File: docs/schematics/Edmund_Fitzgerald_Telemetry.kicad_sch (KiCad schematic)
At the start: 18 parts, among them J1 RC_Receiver, J3 Battery_LiPo, M1 Rudder_Servo, Q1 MOSFET_N, Q2 MOSFET_N, U1 ESP32_Control, U2 MAX98357A, U3 DFPlayer_Pro, U4 ESP32-CAM, U5 UBEC_5V_3A

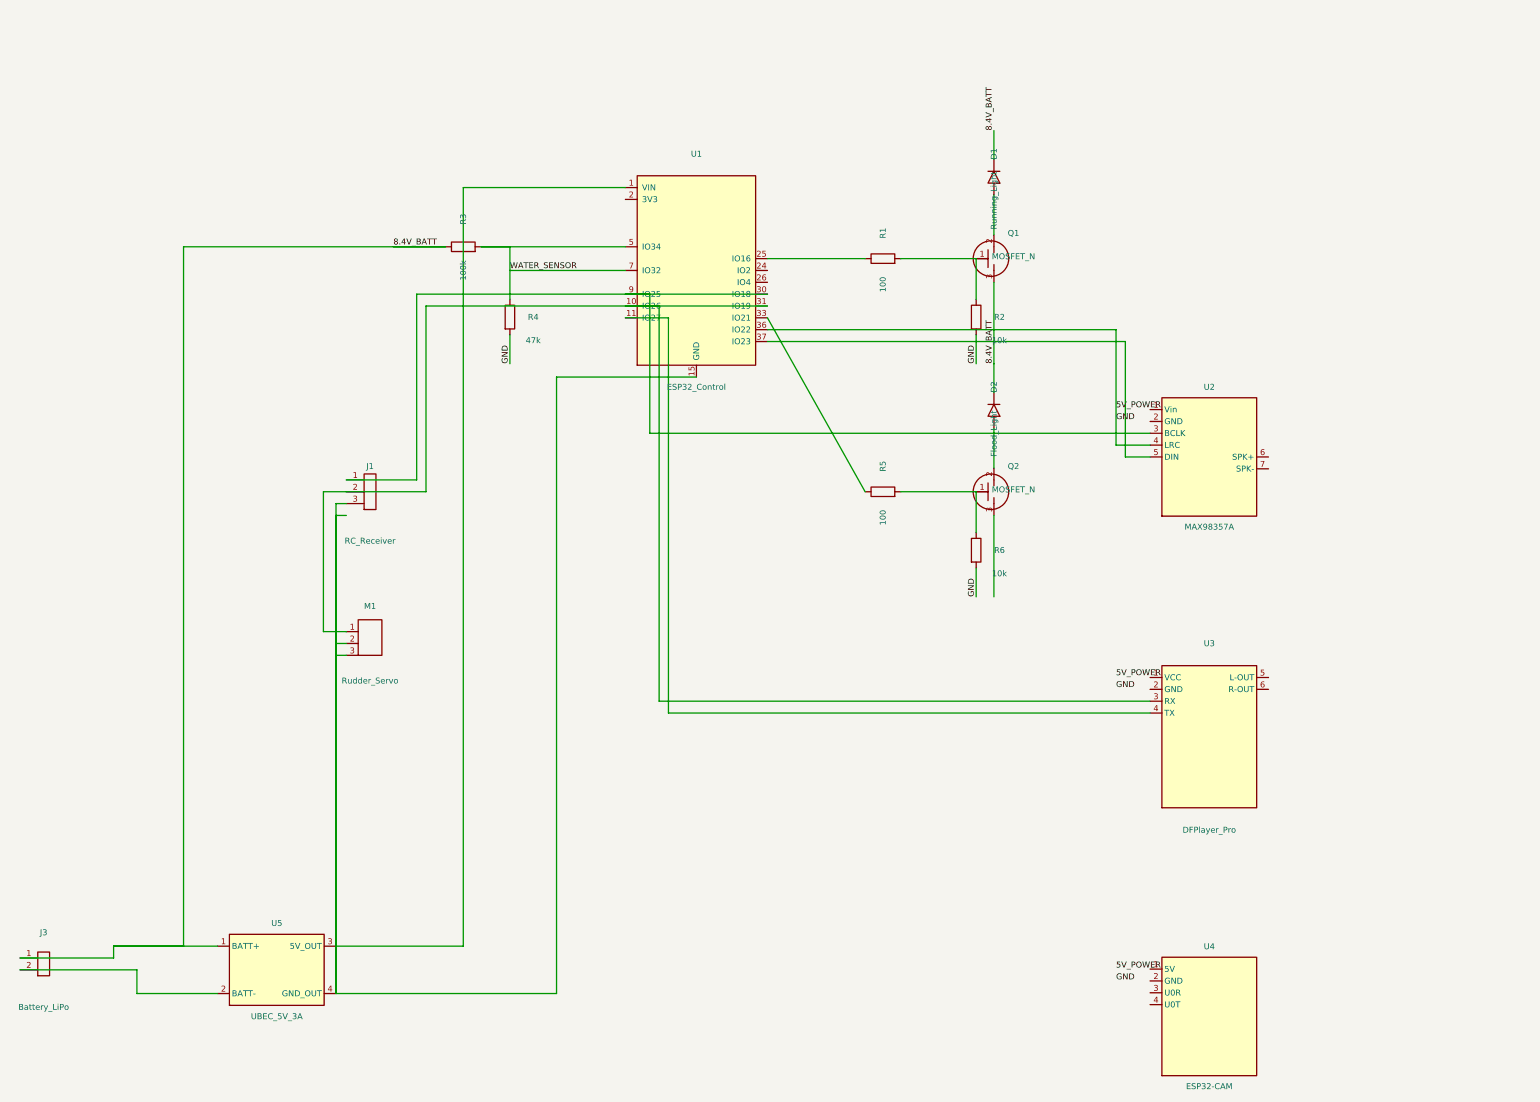
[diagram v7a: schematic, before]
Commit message: Website update: Integrated updated system schematic
- Verified schematic PNG integration in Design and Schematics section
- Committed latest KiCAD schematic source file (v6.0)
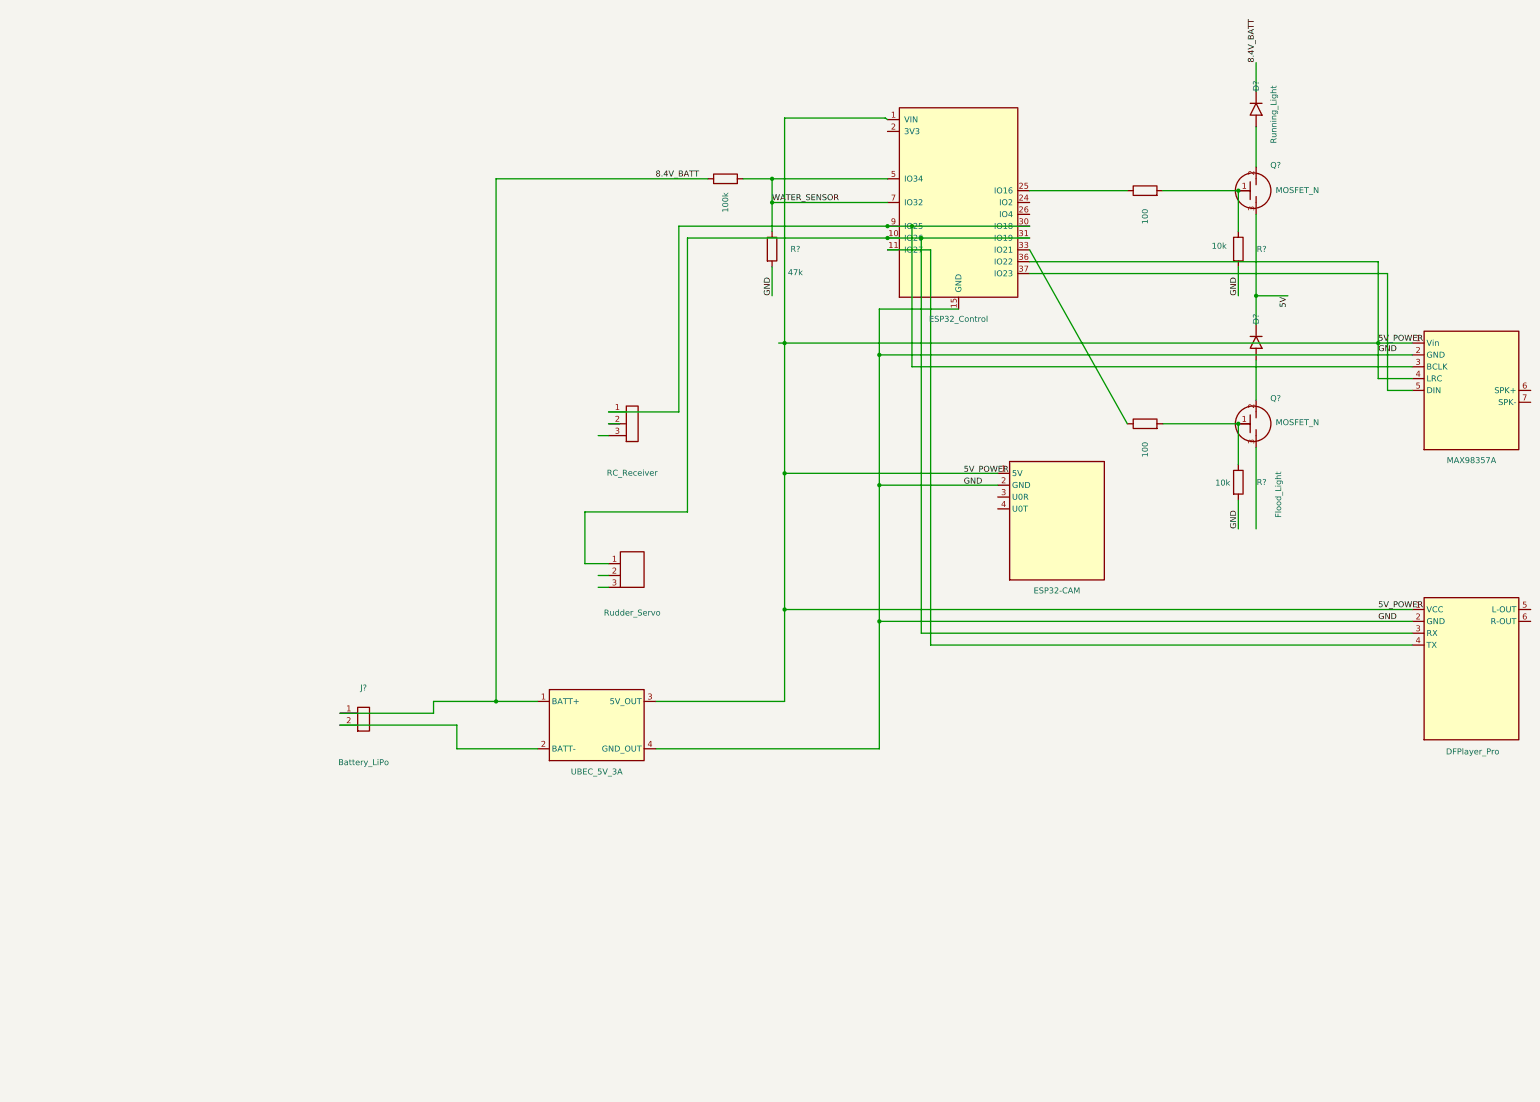
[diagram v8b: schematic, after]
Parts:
- renumbered D2 to D?, D1 to D?, J3 to J?, J1 to J?, M1 to M?, Q2 to Q?, Q1 to Q?, R4 to R?, R2 to R?, R5 to R?, R6 to R?, R3 to R?, R1 to R?, U2 to U?, U3 to U?, U1 to U?, U4 to U?, U5 to U?
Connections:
- net 5V_POWER: now also U?.1 (5V), U?.1 (VCC), U?.1 (VIN), U?.1 (Vin), U?.15 (GND), U?.2 (GND), U?.2 (GND), U?.2 (GND), U?.3 (5V_OUT), U?.4 (GND_OUT)
- net 8.4V_BATT: no longer D?.2 (A), Q?.3 (S)
- net at M?.1 (PWM), U?.10 (IO26), U?.3 (RX)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: no longer J?.2
- new net: D?.2 (A), Q?.3 (S)
- now unconnected: J?.3, M?.2 (VCC), M?.3 (GND)
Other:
- moved on the sheet: D?, J?, Q?, R?
